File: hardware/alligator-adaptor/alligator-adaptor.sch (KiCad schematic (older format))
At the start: 15 parts, among them P1 CONN_01X04, P10 CONN_01X04, P11 CONN_01X04, P2 CONN_02X08, P3 CONN_02X10, P4 CONN_01X04, P5 CONN_01X04, P6 CONN_01X04, P7 CONN_01X04, P8 CONN_01X04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

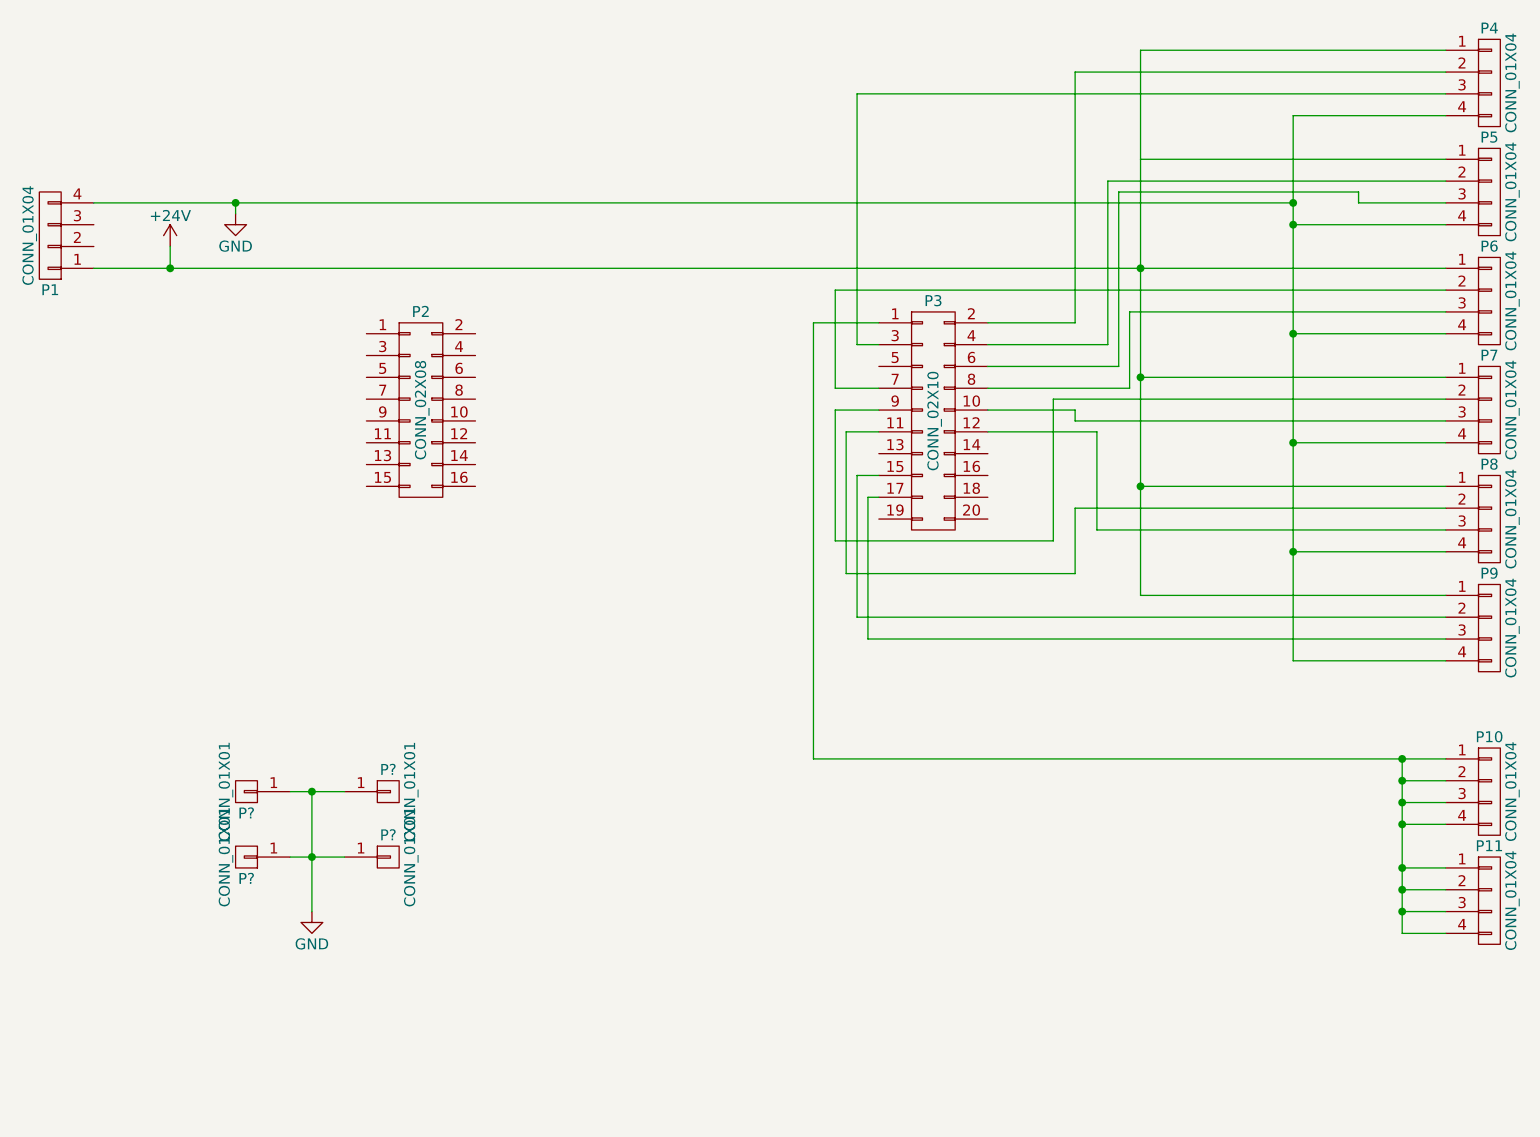
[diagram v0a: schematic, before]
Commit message: First pass at component footprint association.
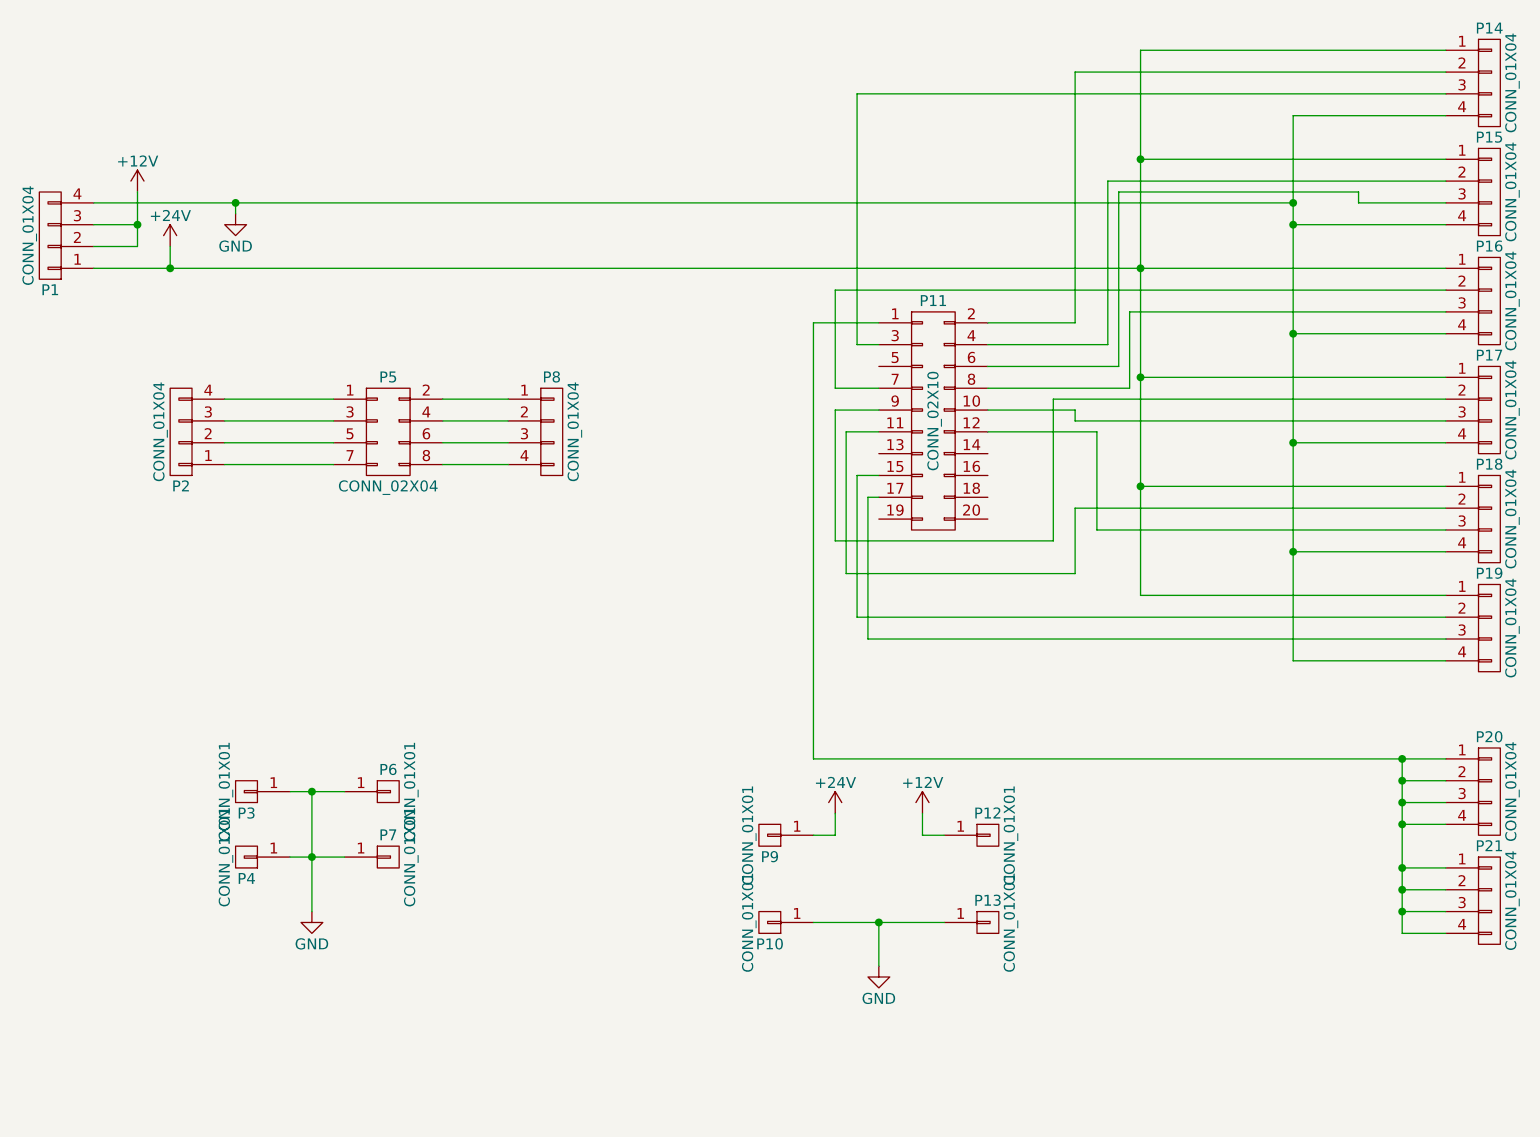
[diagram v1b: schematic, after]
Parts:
- removed P2: CONN_02X08, symbol CONN_02X08
- added P10, P12, P13, P9: CONN_01X01, Wire_Pads:SolderWirePad_single_1mmDrill, symbol CONN_01X01
- added P2, P8: CONN_01X04, Pin_Headers:Pin_Header_Straight_1x04, symbol CONN_01X04
- added P5: CONN_02X04, Pin_Headers:Pin_Header_Straight_2x04_Pitch1.27mm, symbol CONN_02X04
- P1: footprint (none) -> Terminal_Blocks:TerminalBlock_Pheonix_MKDS1.5-4pol
- P11: renamed from P3; footprint (none) -> Pin_Headers:Pin_Header_Straight_2x10
- P14: renamed from P4; footprint (none) -> Terminal_Blocks:TerminalBlock_Pheonix_MKDS1.5-4pol
- P15: renamed from P5; footprint (none) -> Terminal_Blocks:TerminalBlock_Pheonix_MKDS1.5-4pol
- P16: renamed from P6; footprint (none) -> Terminal_Blocks:TerminalBlock_Pheonix_MKDS1.5-4pol
- P17: renamed from P7; footprint (none) -> Terminal_Blocks:TerminalBlock_Pheonix_MKDS1.5-4pol
- P18: renamed from P8; footprint (none) -> Terminal_Blocks:TerminalBlock_Pheonix_MKDS1.5-4pol
- P19: renamed from P9; footprint (none) -> Terminal_Blocks:TerminalBlock_Pheonix_MKDS1.5-4pol
- P20: renamed from P10; footprint (none) -> Terminal_Blocks:TerminalBlock_Pheonix_MKDS1.5-4pol
- P21: renamed from P11; footprint (none) -> Terminal_Blocks:TerminalBlock_Pheonix_MKDS1.5-4pol
- P3, P4, P6, P7: renamed from P?; footprint (none) -> Mounting_Holes:MountingHole_3.2mm_M3_Pad_Via
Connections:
- net +24V: now also P15.1 (P1), P9.1 (P1)
- net GND: now also P10.1 (P1), P13.1 (P1)
- net +12V: now reaches P1.2 (P2)
- net +12V: now also P1.3 (P3), P12.1 (P1)
- new net: P2.4 (P4), P5.1 (P1)
- new net: P5.2 (P2), P8.1 (P1)
- new net: P2.3 (P3), P5.3 (P3)
- new net: P5.4 (P4), P8.2 (P2)
- new net: P2.2 (P2), P5.5 (P5)
- new net: P5.6 (P6), P8.3 (P3)
- new net: P2.1 (P1), P5.7 (P7)
- new net: P5.8 (P8), P8.4 (P4)

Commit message: First pass at footprint selection and layout.
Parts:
- P11: footprint Pin_Headers:Pin_Header_Straight_2x10 -> custom:Pin_Header_Straight_2x10_Pitch1.27mm
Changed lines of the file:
@@
 F 0 "P11" H 5150 3350 50  0000 C CNN
 F 1 "CONN_02X10" V 5150 2800 50  0000 C CNN
-F 2 "Pin_Headers:Pin_Header_Straight_2x10" H 5150 1600 50  0001 C CNN
+F 2 "custom:Pin_Header_Straight_2x10_Pitch1.27mm" H 5150 1600 50  0001 C CNN
 F 3 "" H 5150 1600 50  0000 C CNN
 	1    5150 2800
@@
 Connection ~ 2300 4500
 $Comp
-L GND #PWR4
+L GND #PWR01
 U 1 1 57A9ECB0
 P 2300 5050
-F 0 "#PWR4" H 2300 4800 50  0001 C CNN
+F 0 "#PWR01" H 2300 4800 50  0001 C CNN
 F 1 "GND" H 2300 4900 50  0000 C CNN
 F 2 "" H 2300 5050 50  0000 C CNN
@@
 $EndComp
 $Comp
-L GND #PWR3
+L GND #PWR02
 U 1 1 57A9ED1E
 P 1950 1850
-F 0 "#PWR3" H 1950 1600 50  0001 C CNN
+F 0 "#PWR02" H 1950 1600 50  0001 C CNN
 F 1 "GND" H 1950 1700 50  0000 C CNN
 F 2 "" H 1950 1850 50  0000 C CNN
@@
 Connection ~ 1950 1800
 $Comp
-L +24V #PWR2
+L +24V #PWR03
 U 1 1 57A9F023
 P 1650 2000
-F 0 "#PWR2" H 1650 1850 50  0001 C CNN
+F 0 "#PWR03" H 1650 1850 50  0001 C CNN
 F 1 "+24V" H 1650 2140 50  0000 C CNN
 F 2 "" H 1650 2000 50  0000 C CNN
@@
 Connection ~ 6100 1600
 $Comp
-L +12V #PWR1
+L +12V #PWR04
 U 1 1 57AC7CD9
 P 1500 1750
-F 0 "#PWR1" H 1500 1600 50  0001 C CNN
+F 0 "#PWR04" H 1500 1600 50  0001 C CNN
 F 1 "+12V" H 1500 1890 50  0000 C CNN
 F 2 "" H 1500 1750 50  0000 C CNN
@@
 $EndComp
 $Comp
-L GND #PWR6
+L GND #PWR05
 U 1 1 57AC8CC7
 P 4900 5300
-F 0 "#PWR6" H 4900 5050 50  0001 C CNN
+F 0 "#PWR05" H 4900 5050 50  0001 C CNN
 F 1 "GND" H 4900 5150 50  0000 C CNN
 F 2 "" H 4900 5300 50  0000 C CNN
@@
 Connection ~ 4900 5100
 $Comp
-L +12V #PWR7
+L +12V #PWR06
 U 1 1 57AC8F36
 P 5100 4600
-F 0 "#PWR7" H 5100 4450 50  0001 C CNN
+F 0 "#PWR06" H 5100 4450 50  0001 C CNN
 F 1 "+12V" H 5100 4740 50  0000 C CNN
 F 2 "" H 5100 4600 50  0000 C CNN
@@
 $EndComp
 $Comp
-L +24V #PWR5
+L +24V #PWR07
 U 1 1 57AC8FBD
 P 4700 4600
-F 0 "#PWR5" H 4700 4450 50  0001 C CNN
+F 0 "#PWR07" H 4700 4450 50  0001 C CNN
 F 1 "+24V" H 4700 4740 50  0000 C CNN
 F 2 "" H 4700 4600 50  0000 C CNN

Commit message: First cut.  Routed, zone filled.  Plots generated.
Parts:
- added P22, P23: CONN_01X01, Mounting_Holes:MountingHole_3mm_Pad_Via, symbol CONN_01X01
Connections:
- net GND: now also P22.1 (P1), P23.1 (P1)
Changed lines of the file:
@@
 Wire Wire Line
 	5100 4700 5100 4600
+$Comp
+L CONN_01X01 P23
+U 1 1 57B5A32D
+P 3400 5600
+F 0 "P23" H 3400 5700 50  0000 C CNN
+F 1 "CONN_01X01" V 3500 5600 50  0000 C CNN
+F 2 "Mounting_Holes:MountingHole_3mm_Pad_Via" H 3400 5600 50  0001 C CNN
+F 3 "" H 3400 5600 50  0000 C CNN
+	1    3400 5600
+	1    0    0    -1
+$EndComp
+$Comp
+L CONN_01X01 P22
+U 1 1 57B5A38E
+P 2800 5600
+F 0 "P22" H 2800 5700 50  0000 C CNN
+F 1 "CONN_01X01" V 2900 5600 50  0000 C CNN
+F 2 "Mounting_Holes:MountingHole_3mm_Pad_Via" H 2800 5600 50  0001 C CNN
+F 3 "" H 2800 5600 50  0000 C CNN
+	1    2800 5600
+	-1   0    0    1
+$EndComp
+$Comp
+L GND #PWR08
+U 1 1 57B5A419
+P 3100 5800
+F 0 "#PWR08" H 3100 5550 50  0001 C CNN
+F 1 "GND" H 3100 5650 50  0000 C CNN
+F 2 "" H 3100 5800 50  0000 C CNN
+F 3 "" H 3100 5800 50  0000 C CNN
+	1    3100 5800
+	1    0    0    -1
+$EndComp
+Wire Wire Line
+	3000 5600 3200 5600
+Wire Wire Line
+	3100 5600 3100 5800
+Connection ~ 3100 5600
 $EndSCHEMATC
